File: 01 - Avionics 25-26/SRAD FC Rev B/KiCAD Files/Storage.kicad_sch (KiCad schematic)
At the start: 5 parts

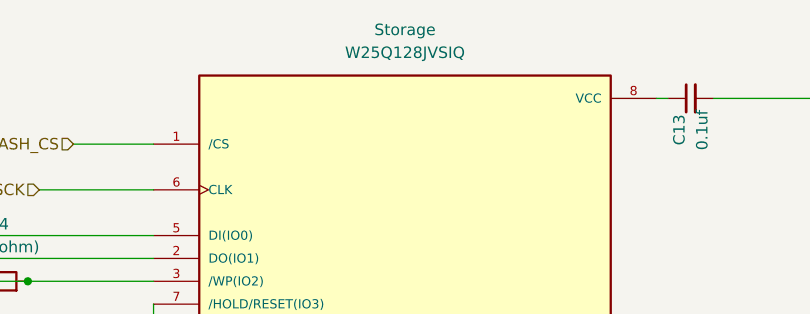
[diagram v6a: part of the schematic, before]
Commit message: set up power conversion, wired power to mcu
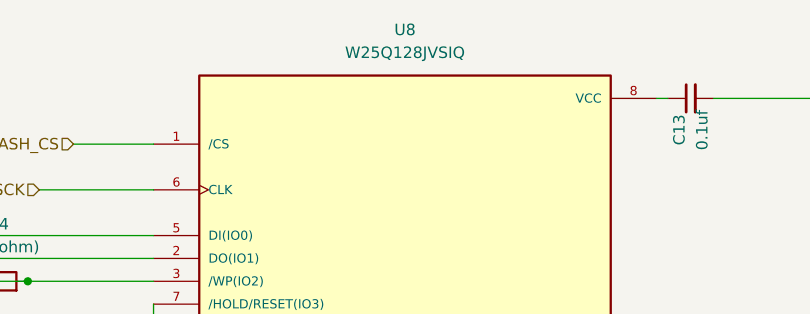
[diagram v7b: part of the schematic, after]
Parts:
- removed Storage: W25Q128JVSIQ, W25Q128JVSIQ:SOIC127P790X216-8N, symbol W25Q128JVSIQ:W25Q128JVSIQ
- added U8: W25Q128JVSIQ, W25Q128JVSIQ:SOIC127P790X216-8N, symbol W25Q128JVSIQ:W25Q128JVSIQ
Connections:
- net FLASH_3.3V_POWER: now also U8.3 (/WP(IO2))
- net FLASH_CS: now also U8.1 (/CS)
- net FLASH_MISO: now also U8.2 (DO(IO1))
- net FLASH_MOSI: now also U8.5 (DI(IO0))
- net FLASH_SCK: now also U8.6 (CLK)
- net at C14.1: now also U8.4 (GND)
- net at R105.2: now also U8.7 (/HOLD/RESET(IO3))
- net at C13.1: now also U8.8 (VCC)
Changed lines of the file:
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@@
-	)
-	(symbol
-		(lib_id "W25Q128JVSIQ:W25Q128JVSIQ")
-		(at 144.78 90.17 0)
-		(unit 1)
-		(exclude_from_sim no)
-		(in_bom yes)
-		(on_board yes)
-		(dnp no)
-		(fields_autoplaced yes)
-		(property "Reference" "Storage"
-			(at 144.78 69.85 0)
-			(effects
-				(font
-					(size 1.27 1.27)
-				)
-			)
-		)
-		(property "Value" "W25Q128JVSIQ"
-			(at 144.78 72.39 0)
-			(effects
-				(font
-					(size 1.27 1.27)
-				)
-			)
-		)
-		(property "Footprint" "W25Q128JVSIQ:SOIC127P790X216-8N"
-			(at 144.78 90.17 0)
-			(effects
-				(font
-					(size 1.27 1.27)
-				)
-				(justify bottom)
-				(hide yes)
-			)
-		)
-		(property "Datasheet" "https://mm.digikey.com/Volume0/opasdata/d220001/medias/docus/7161/256_W25Q128JV.pdf"
-			(at 144.78 90.17 0)
-			(effects
-				(font
-					(size 1.27 1.27)
-				)
-				(hide yes)
-			)
-		)
-		(property "Description" "3V 128M-BIT  SERIAL FLASH MEMORY WITH   DUAL/QUAD SPI"
-			(at 144.78 90.17 0)
-			(effects
-				(font
-					(size 1.27 1.27)
-				)
-				(hide yes)
-			)
-		)
-		(property "Link" "https://www.digikey.com/en/products/detail/winbond-electronics/W25Q128JVSIQ/5803943"
-			(at 144.78 90.17 0)
-			(effects
-				(font
-					(size 1.27 1.27)
-				)
-				(hide yes)
-			)
-		)
-		(property "PARTREV" "I"
-			(at 144.78 90.17 0)
-			(effects
-				(font
-					(size 1.27 1.27)
-				)
-				(justify bottom)
-				(hide yes)
-			)
-		)
-		(property "STANDARD" "IPC-7351B"
-			(at 144.78 90.17 0)
-			(effects
-				(font
-					(size 1.27 1.27)
-				)
-				(justify bottom)
-				(hide yes)
-			)
-		)
-		(property "MAXIMUM_PACKAGE_HEIGHT" "2.16 mm"
-			(at 144.78 90.17 0)
-			(effects
-				(font
-					(size 1.27 1.27)
-				)
-				(justify bottom)
-				(hide yes)
-			)
-		)
-		(property "MANUFACTURER" "Winbond Electronics"
-			(at 144.78 90.17 0)
-			(effects
-				(font
-					(size 1.27 1.27)
-				)
-				(justify bottom)
-				(hide yes)
-			)
-		)
-		(pin "1"
-		)
-		(pin "6"
-		)
-		(pin "4"
-		)
-		(pin "7"
-		)
-		(pin "5"
-		)
-		(pin "2"
-		)
-		(pin "3"
-		)
-		(pin "8"
-		)
-		(instances
-			(project ""
-				(path "/1dd9e63a-24f2-43c6-ae21-66b89e6998f2/7a96f78f-7769-410f-82f2-b37baf0f0866"
-					(reference "Storage")
-					(unit 1)
-				)
-			)
-		)
 	)
 	(symbol
@@
 					(unit 1)
 				)
+			)
+		)
+	)
+	(symbol
+		(lib_id "W25Q128JVSIQ:W25Q128JVSIQ")
+		(at 144.78 90.17 0)
+		(unit 1)
+		(exclude_from_sim no)
+		(in_bom yes)
+		(on_board yes)
+		(dnp no)
+		(fields_autoplaced yes)
+		(property "Reference" "U8"
+			(at 144.78 69.85 0)
+			(effects
+				(font
+					(size 1.27 1.27)
+				)
+			)
+		)
+		(property "Value" "W25Q128JVSIQ"
+			(at 144.78 72.39 0)
+			(effects
+				(font
+					(size 1.27 1.27)
+				)
+			)
+		)
+		(property "Footprint" "W25Q128JVSIQ:SOIC127P790X216-8N"
+			(at 144.78 90.17 0)
+			(effects
+				(font
+					(size 1.27 1.27)
+				)
+				(justify bottom)
+				(hide yes)
+			)
+		)
+		(property "Datasheet" ""
+			(at 144.78 90.17 0)
+			(effects
+				(font
+					(size 1.27 1.27)
+				)
+				(hide yes)
+			)
+		)
+		(property "Description" ""
+			(at 144.78 90.17 0)
+			(effects
+				(font
+					(size 1.27 1.27)
+				)
+				(hide yes)
+			)
+		)
+		(property "PARTREV" "I"
+			(at 144.78 90.17 0)
+			(effects
+				(font
+					(size 1.27 1.27)
+				)
+				(justify bottom)
+				(hide yes)
+			)
+		)
+		(property "STANDARD" "IPC-7351B"
+			(at 144.78 90.17 0)
+			(effects
+				(font
+					(size 1.27 1.27)
+				)
+				(justify bottom)
+				(hide yes)
+			)
+		)
+		(property "MAXIMUM_PACKAGE_HEIGHT" "2.16 mm"
+			(at 144.78 90.17 0)
+			(effects
+				(font
+					(size 1.27 1.27)
+				)
+				(justify bottom)
+				(hide yes)
+			)
+		)
+		(property "MANUFACTURER" "Winbond Electronics"
+			(at 144.78 90.17 0)
+			(effects
+				(font
+					(size 1.27 1.27)
+				)
+				(justify bottom)
+				(hide yes)
+			)
+		)
+		(pin "2"
+		)
+		(pin "8"
+		)
+		(pin "1"
+		)
+		(pin "6"
+		)
+		(pin "7"
+		)
+		(pin "5"
+		)
+		(pin "3"
+		)
+		(pin "4"
+		)
+		(instances
+			(project ""
+				(path "/1dd9e63a-24f2-43c6-ae21-66b89e6998f2/7a96f78f-7769-410f-82f2-b37baf0f0866"
+					(reference "U8")
+					(unit 1)
+				)

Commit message: more changes based on seth's feedback
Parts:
- removed C14: 4.7uf, symbol Device:C_Small
- added R3: R (100kohm), symbol Device:R
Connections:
- net FLASH_3.3V_POWER: now also U8.8 (VCC), R3.2; no longer R14.2, U8.3 (/WP(IO2))
- net FLASH_CS: now also R3.1
- net GND: now also C13.1, U8.4 (GND)
- new net: R14.2, U8.3 (/WP(IO2))
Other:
- moved on the sheet: C13
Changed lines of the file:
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@@
 	)
 	(junction
-		(at 95.25 97.79)
+		(at 176.53 77.47)
 		(diameter 0)
 		(color 0 0 0 0)
@@
 	)
 	(junction
-		(at 102.87 97.79)
+		(at 143.51 124.46)
 		(diameter 0)
 		(color 0 0 0 0)
 	)
-	(wire
-		(pts
-			(xy 95.25 97.79) (xy 102.87 97.79)
+	(junction
+		(at 114.3 82.55)
+		(diameter 0)
+		(color 0 0 0 0)
+	)
+	(wire
+		(pts
+			(xy 176.53 93.98) (xy 176.53 86.36)
+		)
+		(stroke
+			(width 0)
+			(type default)
+		)
+	)
+	(wire
+		(pts
+			(xy 143.51 124.46) (xy 143.51 133.35)
 		)
 		(stroke
@@
 	(wire
 		(pts
+			(xy 176.53 77.47) (xy 172.72 77.47)
+		)
+		(stroke
+			(width 0)
+			(type default)
+		)
+	)
+	(wire
+		(pts
+			(xy 114.3 71.12) (xy 114.3 63.5)
+		)
+		(stroke
+			(width 0)
+			(type default)
+		)
+	)
+	(wire
+		(pts
 			(xy 85.09 92.71) (xy 116.84 92.71)
 		)
@@
 	(wire
 		(pts
+			(xy 176.53 109.22) (xy 176.53 105.41)
+		)
+		(stroke
+			(width 0)
+			(type default)
+		)
+	)
+	(wire
+		(pts
 			(xy 116.84 100.33) (xy 116.84 113.03)
 		)
@@
 	(wire
 		(pts
-			(xy 179.07 77.47) (xy 199.39 77.47)
+			(xy 62.23 63.5) (xy 62.23 124.46)
 		)
 		(stroke
@@
 	(wire
 		(pts
-			(xy 143.51 123.19) (xy 143.51 133.35)
+			(xy 143.51 123.19) (xy 143.51 124.46)
+		)
+		(stroke
+			(width 0)
+			(type default)
+		)
+	)
+	(wire
+		(pts
+			(xy 62.23 124.46) (xy 143.51 124.46)
 		)
 		(stroke
@@
 	(wire
 		(pts
-			(xy 172.72 77.47) (xy 173.99 77.47)
-		)
-		(stroke
-			(width 0)
-			(type default)
-		)
-	)
-	(wire
-		(pts
-			(xy 107.95 82.55) (xy 116.84 82.55)
+			(xy 176.53 77.47) (xy 199.39 77.47)
+		)
+		(stroke
+			(width 0)
+			(type default)
+		)
+	)
+	(wire
+		(pts
+			(xy 114.3 63.5) (xy 62.23 63.5)
+		)
+		(stroke
+			(width 0)
+			(type default)
+		)
+	)
+	(wire
+		(pts
+			(xy 114.3 82.55) (xy 116.84 82.55)
+		)
+		(stroke
+			(width 0)
+			(type default)
+		)
+	)
+	(wire
+		(pts
+			(xy 107.95 82.55) (xy 114.3 82.55)
+		)
+		(stroke
+			(width 0)
+			(type default)
+		)
+	)
+	(wire
+		(pts
+			(xy 114.3 78.74) (xy 114.3 82.55)
 		)
 		(stroke
@@
 		(pts
 			(xy 95.25 104.14) (xy 95.25 113.03)
+		)
+		(stroke
+			(width 0)
+			(type default)
+		)
+	)
+	(wire
+		(pts
+			(xy 176.53 81.28) (xy 176.53 77.47)
+		)
+		(stroke
+			(width 0)
+			(type default)
+		)
+	)
+	(wire
+		(pts
+			(xy 176.53 105.41) (xy 172.72 105.41)
 		)
 		(stroke
@@
 	(symbol
 		(lib_id "power:GND")
-		(at 177.8 105.41 90)
+		(at 176.53 109.22 0)
 		(unit 1)
 		(exclude_from_sim no)
@@
 		(fields_autoplaced yes)
 		(property "Reference" "#PWR020"
-			(at 184.15 105.41 0)
+			(at 176.53 115.57 0)
 			(effects
 				(font
@@
 		)
 		(property "Value" "GND"
-			(at 181.61 105.4099 90)
-			(effects
-				(font
-					(size 1.27 1.27)
-				)
-				(justify right)
+			(at 179.07 110.4899 0)
+			(effects
+				(font
+					(size 1.27 1.27)
+				)
+				(justify left)
 			)
 		)
 		(property "Footprint" ""
-			(at 177.8 105.41 0)
+			(at 176.53 109.22 0)
 			(effects
 				(font
@@
 		)
 		(property "Datasheet" ""
-			(at 177.8 105.41 0)
+			(at 176.53 109.22 0)
 			(effects
 				(font
@@
 		)
 		(property "Description" "Power symbol creates a global label with name \"GND\" , ground"
-			(at 177.8 105.41 0)
+			(at 176.53 109.22 0)
 			(effects
 				(font
@@
 	(symbol
 		(lib_id "Device:R")
+		(at 114.3 74.93 180)
+		(unit 1)
+		(exclude_from_sim no)
+		(in_bom yes)
+		(on_board yes)
+		(dnp no)
+		(fields_autoplaced yes)
+		(property "Reference" "R3"
+			(at 116.84 73.6599 0)
+			(effects
+				(font
+					(size 1.27 1.27)
+				)
+				(justify right)
+			)
+		)
+		(property "Value" "R (100kohm)"
+			(at 116.84 76.1999 0)
+			(effects
+				(font
+					(size 1.27 1.27)
+				)
+				(justify right)
+			)
+		)
+		(property "Footprint" ""
+			(at 116.078 74.93 90)
+			(effects
+				(font
+					(size 1.27 1.27)
+				)
+				(hide yes)
+			)
+		)
+		(property "Datasheet" "~"
+			(at 114.3 74.93 0)
+			(effects
+				(font
+					(size 1.27 1.27)
+				)
+				(hide yes)
+			)
+		)
+		(property "Description" "Resistor"
+			(at 114.3 74.93 0)
+			(effects
+				(font
+					(size 1.27 1.27)
+				)
+				(hide yes)
+			)
+		)
+		(pin "1"
+		)
+		(pin "2"
+		)
+		(instances
+			(project "SRAD FC Rev B"
+				(path "/1dd9e63a-24f2-43c6-ae21-66b89e6998f2/7a96f78f-7769-410f-82f2-b37baf0f0866"
+					(reference "R3")
+					(unit 1)
+				)
+			)
+		)
+	)
+	(symbol
+		(lib_id "Device:R")
 		(at 99.06 97.79 90)
 		(unit 1)
@@
 	)
 	(symbol
-		(lib_id "Device:C_Small")
-		(at 175.26 105.41 90)
-		(mirror x)
+		(lib_id "power:GND")
+		(at 176.53 93.98 0)
 		(unit 1)
 		(exclude_from_sim no)
@@
 		(on_board yes)
 		(dnp no)
-		(property "Reference" "C14"
-			(at 173.99 107.188 0)
+		(fields_autoplaced yes)
+		(property "Reference" "#PWR05"
+			(at 176.53 100.33 0)
+			(effects
+				(font
+					(size 1.27 1.27)
+				)
+				(hide yes)
+			)
+		)
+		(property "Value" "GND"
+			(at 179.07 95.2499 0)
 			(effects
 				(font
@@
 			)
 		)
-		(property "Value" "4.7uf"
-			(at 176.53 106.68 0)
-			(effects
-				(font
-					(size 1.27 1.27)
-				)
-				(justify left)
-			)
-		)
 		(property "Footprint" ""
-			(at 175.26 105.41 0)
-			(effects
-				(font
-					(size 1.27 1.27)
-				)
-				(hide yes)
-			)
-		)
-		(property "Datasheet" "~"
-			(at 175.26 105.41 0)
-			(effects
-				(font
-					(size 1.27 1.27)
-				)
-				(hide yes)
-			)
-		)
-		(property "Description" "Unpolarized capacitor, small symbol"
-			(at 175.26 105.41 0)
-			(effects
-				(font
-					(size 1.27 1.27)
-				)
-				(hide yes)
-			)
-		)
-		(pin "2"
+			(at 176.53 93.98 0)
+			(effects
+				(font
+					(size 1.27 1.27)
+				)
+				(hide yes)
+			)
+		)
+		(property "Datasheet" ""
+			(at 176.53 93.98 0)
+			(effects
+				(font
+					(size 1.27 1.27)
+				)
+				(hide yes)
+			)
+		)
+		(property "Description" "Power symbol creates a global label with name \"GND\" , ground"
+			(at 176.53 93.98 0)
+			(effects
+				(font
+					(size 1.27 1.27)
+				)
+				(hide yes)
+			)
 		)
 		(pin "1"
@@
 			(project "SRAD FC Rev B"
 				(path "/1dd9e63a-24f2-43c6-ae21-66b89e6998f2/7a96f78f-7769-410f-82f2-b37baf0f0866"
-					(reference "C14")
+					(reference "#PWR05")
 					(unit 1)
 				)
@@
 	(symbol
 		(lib_id "Device:C_Small")
-		(at 176.53 77.47 90)
+		(at 176.53 83.82 0)
 		(mirror x)
 		(unit 1)
@@
 		(dnp no)
 		(property "Reference" "C13"
-			(at 175.26 79.248 0)
+			(at 178.308 85.09 0)
 			(effects
 				(font
@@
 		)
 		(property "Value" "0.1uf"
-			(at 177.8 78.74 0)
+			(at 177.8 82.55 0)
 			(effects
 				(font
@@
 		)
 		(property "Footprint" ""
-			(at 176.53 77.47 0)
+			(at 176.53 83.82 0)
 			(effects
 				(font
@@
 		)
 		(property "Datasheet" "~"
-			(at 176.53 77.47 0)
+			(at 176.53 83.82 0)
 			(effects
 				(font
@@
 		)
 		(property "Description" "Unpolarized capacitor, small symbol"
-			(at 176.53 77.47 0)
-			(effects
-				(font
+			(at 176.53 83.82 0)
+			(effects
+				(font
